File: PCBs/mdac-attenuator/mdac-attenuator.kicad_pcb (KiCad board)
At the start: 2 copper layers, 45.7 x 52.1 mm, 34 parts, among them J1 Conn_01x06_Male, J2 Conn_01x06_Male, U1 AD8599, U2 DAC8812ICPWG4

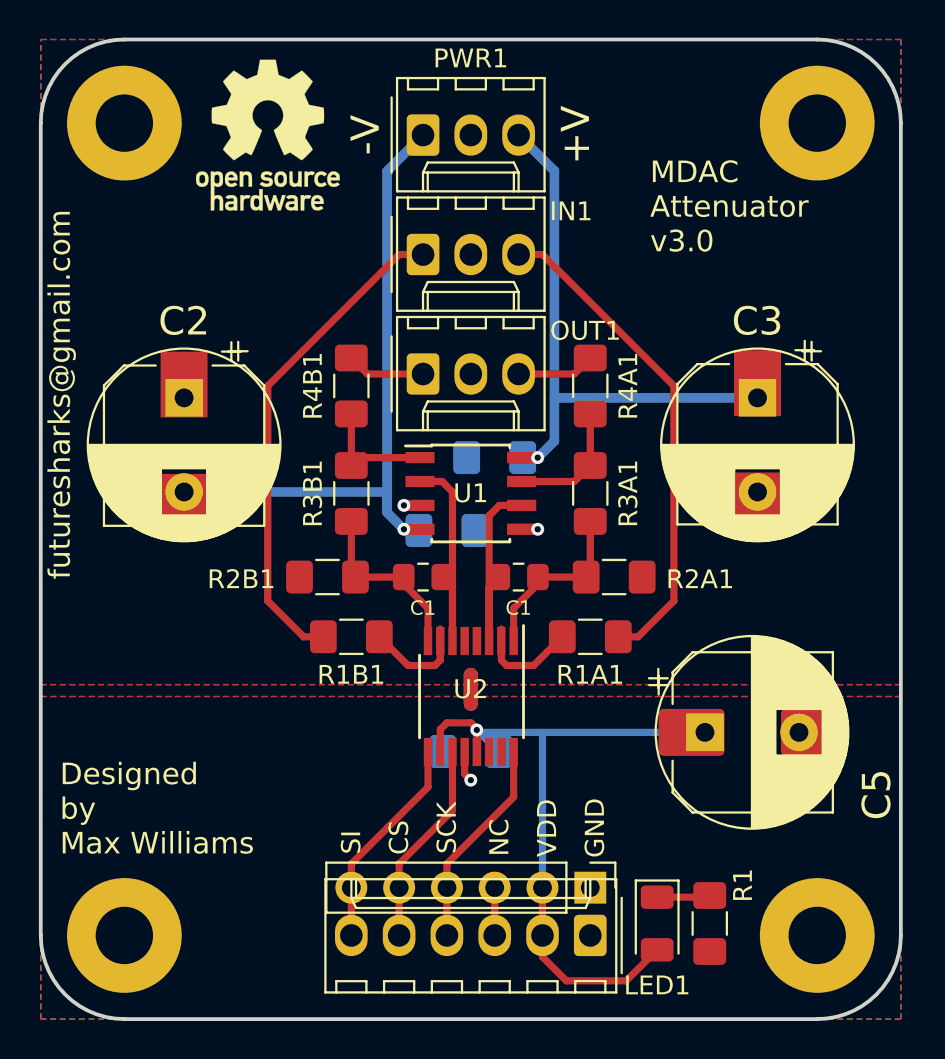
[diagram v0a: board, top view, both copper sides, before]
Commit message: Updated the mdac-attenuator to work with kicad 5.
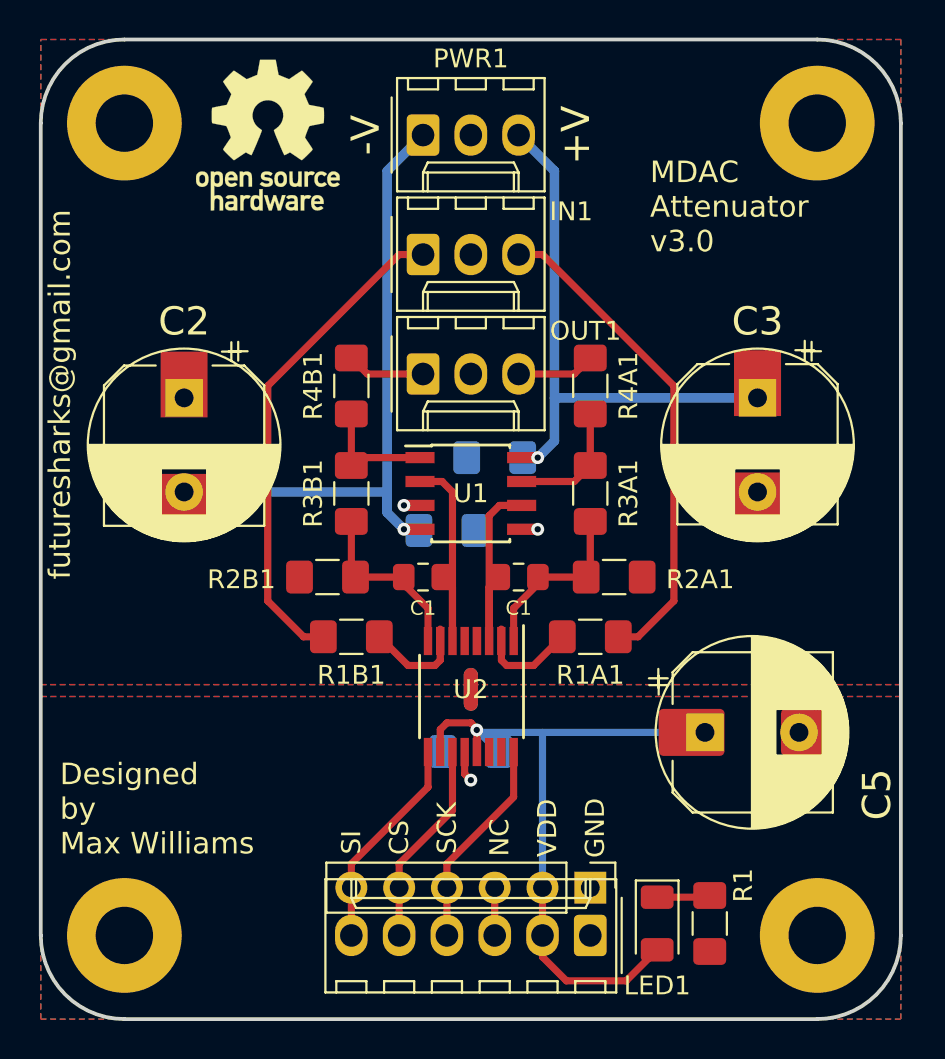
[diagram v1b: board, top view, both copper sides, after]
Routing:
- net -15V: track 35.5 -> 36.4 mm
- net +15V: track 29.9 -> 30.8 mm
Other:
- rule solder_mask_min_width: 0.25 -> 0.101
